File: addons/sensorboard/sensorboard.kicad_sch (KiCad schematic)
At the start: 13 parts, among them J1 Conn_02x06_Odd_Even, J10 Adafruit_I2C_Header, J11 BME680_Header, J12 RGB_Header, J2 SparkFun_I2C_Header, J3 Adafruit_I2C_Header, J4 Pimoroni_I2CGarden_Header, J5 Pimoroni_I2CGarden_Header, J6 Adafruit_I2C_Header, J7 SparkFun_I2C_Header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

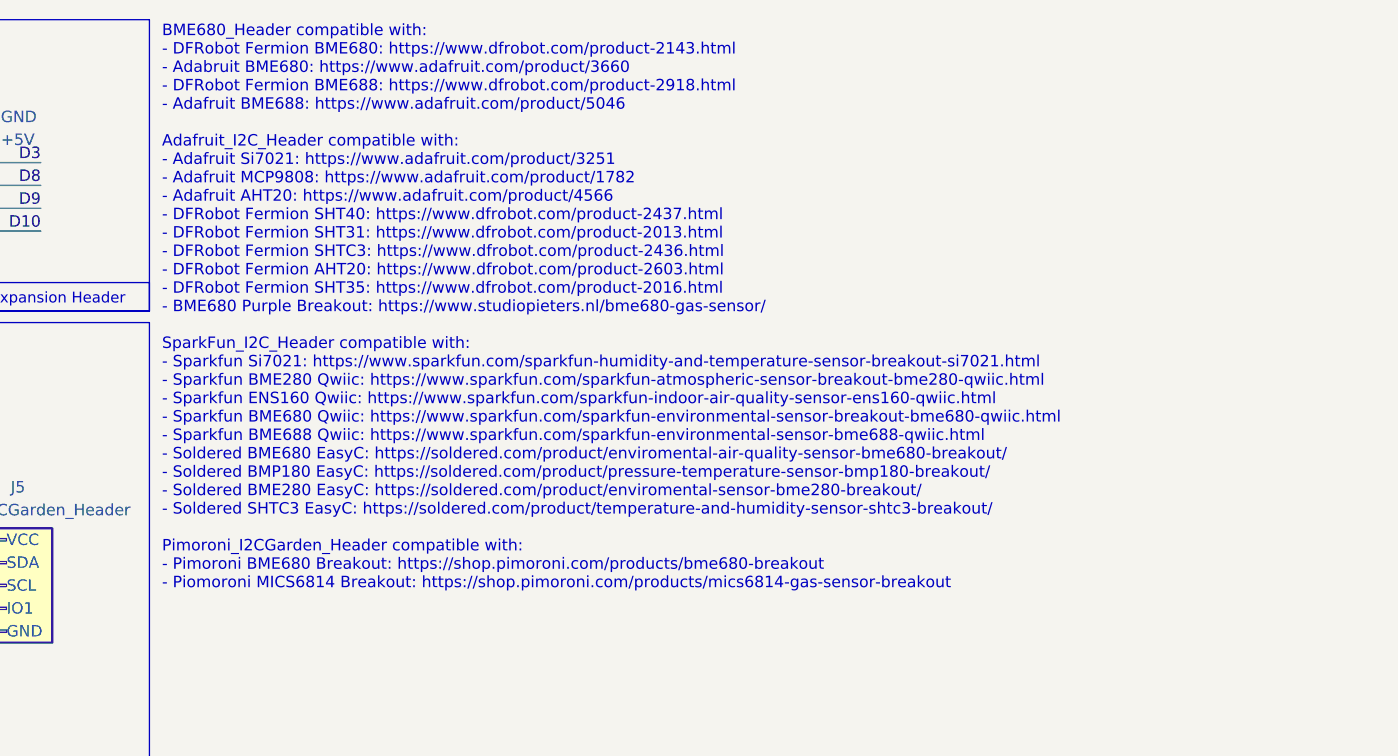
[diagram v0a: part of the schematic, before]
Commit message: More compact version of the AQStation
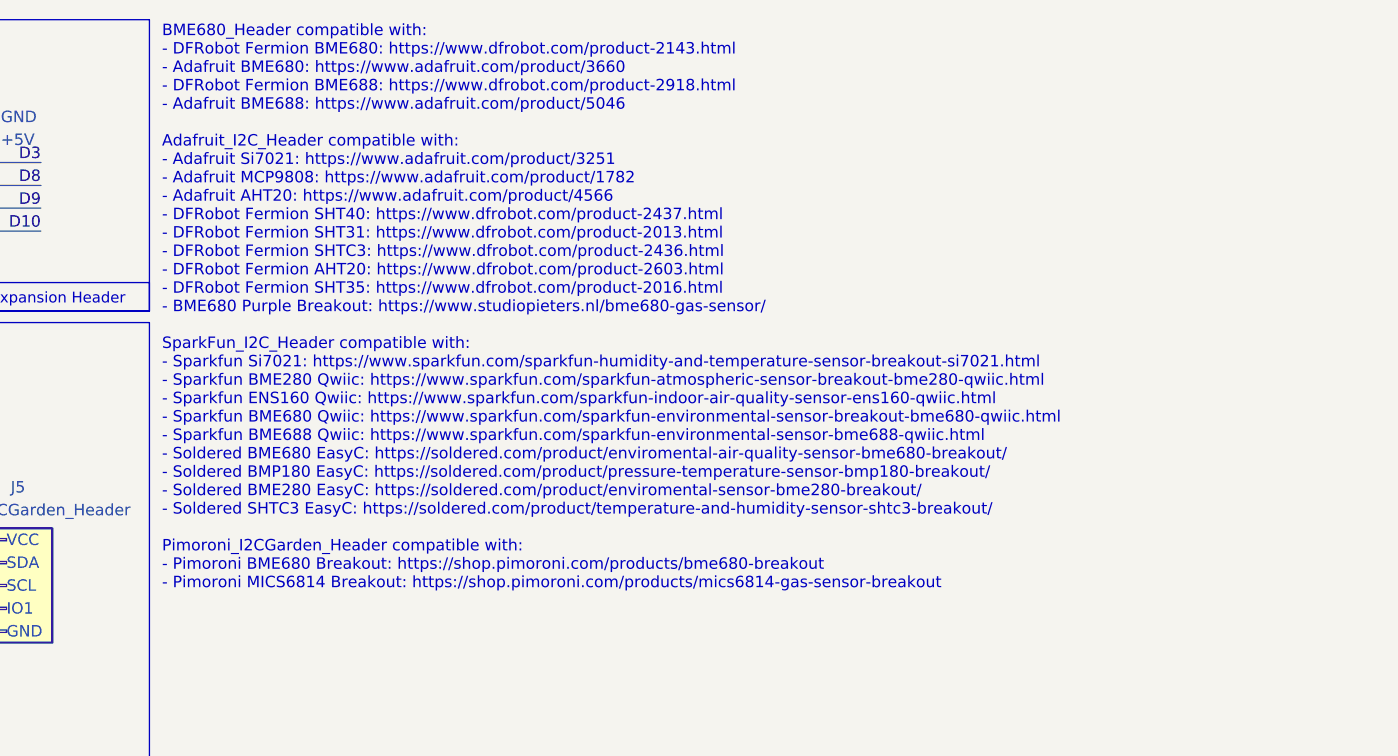
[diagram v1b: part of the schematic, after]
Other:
- note added: "BME680_Header compatible with: - DFRobot Fermion BME680: https://www.dfrobot.com/product-2143.html - Adafruit BME680: https://www.adafruit.com/product/3660 - DFRobot Fermion BME688: https://www.dfrobot.com/product-2918.html - Adafruit BME688: https://www.adafruit.com/product/5046 Adafruit_I2C_Header compatible with: - Adafruit Si7021: https://www.adafruit.com/product/3251 - Adafruit MCP9808: http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"
- note removed: "BME680_Header compatible with: - DFRobot Fermion BME680: https://www.dfrobot.com/product-2143.html - Adabruit BME680: https://www.adafruit.com/product/3660 - DFRobot Fermion BME688: https://www.dfrobot.com/product-2918.html - Adafruit BME688: https://www.adafruit.com/product/5046 Adafruit_I2C_Header compatible with: - Adafruit Si7021: https://www.adafruit.com/product/3251 - Adafruit MCP9808: http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"
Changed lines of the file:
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@@
 		)
 	)
-	(text "BME680_Header compatible with:\n- DFRobot Fermion BME680: https://www.dfrobot.com/product-2143.html\n- Adabruit BME680: https://www.adafruit.com/product/3660\n- DFRobot Fermion BME688: https://www.dfrobot.com/product-2918.html\n- Adafruit BME688: https://www.adafruit.com/product/5046\n\nAdafruit_I2C_Header compatible with:\n- Adafruit Si7021: https://www.adafruit.com/product/3251\n- Adafruit MCP9808: https://www.adafruit.com/product/1782\n- Adafruit AHT20: https://www.adafruit.com/product/4566\n- DFRobot Fermion SHT40: https://www.dfrobot.com/product-2437.html\n- DFRobot Fermion SHT31: https://www.dfrobot.com/product-2013.html\n- DFRobot Fermion SHTC3: https://www.dfrobot.com/product-2436.html\n- DFRobot Fermion AHT20: https://www.dfrobot.com/product-2603.html\n- DFRobot Fermion SHT35: https://www.dfrobot.com/product-2016.html\n- BME680 Purple Breakout: https://www.studiopieters.nl/bme680-gas-sensor/\n\nSparkFun_I2C_Header compatible with:\n- Sparkfun Si7021: https://www.sparkfun.com/sparkfun-humidity-and-temperature-sensor-breakout-si7021.html\n- Sparkfun BME280 Qwiic: https://www.sparkfun.com/sparkfun-atmospheric-sensor-breakout-bme280-qwiic.html\n- Sparkfun ENS160 Qwiic: https://www.sparkfun.com/sparkfun-indoor-air-quality-sensor-ens160-qwiic.html\n- Sparkfun BME680 Qwiic: https://www.sparkfun.com/sparkfun-environmental-sensor-breakout-bme680-qwiic.html\n- Sparkfun BME688 Qwiic: https://www.sparkfun.com/sparkfun-environmental-sensor-bme688-qwiic.html\n- Soldered BME680 EasyC: https://soldered.com/product/enviromental-air-quality-sensor-bme680-breakout/\n- Soldered BMP180 EasyC: https://soldered.com/product/pressure-temperature-sensor-bmp180-breakout/\n- Soldered BME280 EasyC: https://soldered.com/product/enviromental-sensor-bme280-breakout/\n- Soldered SHTC3 EasyC: https://soldered.com/product/temperature-and-humidity-sensor-shtc3-breakout/\n\nPimoroni_I2CGarden_Header compatible with:\n- Pimoroni BME680 Breakout: https://shop.pimoroni.com/products/bme680-breakout\n- Piomoroni MICS6814 Breakout: https://shop.pimoroni.com/products/mics6814-gas-sensor-breakout"
+	(text "BME680_Header compatible with:\n- DFRobot Fermion BME680: https://www.dfrobot.com/product-2143.html\n- Adafruit BME680: https://www.adafruit.com/product/3660\n- DFRobot Fermion BME688: https://www.dfrobot.com/product-2918.html\n- Adafruit BME688: https://www.adafruit.com/product/5046\n\nAdafruit_I2C_Header compatible with:\n- Adafruit Si7021: https://www.adafruit.com/product/3251\n- Adafruit MCP9808: https://www.adafruit.com/product/1782\n- Adafruit AHT20: https://www.adafruit.com/product/4566\n- DFRobot Fermion SHT40: https://www.dfrobot.com/product-2437.html\n- DFRobot Fermion SHT31: https://www.dfrobot.com/product-2013.html\n- DFRobot Fermion SHTC3: https://www.dfrobot.com/product-2436.html\n- DFRobot Fermion AHT20: https://www.dfrobot.com/product-2603.html\n- DFRobot Fermion SHT35: https://www.dfrobot.com/product-2016.html\n- BME680 Purple Breakout: https://www.studiopieters.nl/bme680-gas-sensor/\n\nSparkFun_I2C_Header compatible with:\n- Sparkfun Si7021: https://www.sparkfun.com/sparkfun-humidity-and-temperature-sensor-breakout-si7021.html\n- Sparkfun BME280 Qwiic: https://www.sparkfun.com/sparkfun-atmospheric-sensor-breakout-bme280-qwiic.html\n- Sparkfun ENS160 Qwiic: https://www.sparkfun.com/sparkfun-indoor-air-quality-sensor-ens160-qwiic.html\n- Sparkfun BME680 Qwiic: https://www.sparkfun.com/sparkfun-environmental-sensor-breakout-bme680-qwiic.html\n- Sparkfun BME688 Qwiic: https://www.sparkfun.com/sparkfun-environmental-sensor-bme688-qwiic.html\n- Soldered BME680 EasyC: https://soldered.com/product/enviromental-air-quality-sensor-bme680-breakout/\n- Soldered BMP180 EasyC: https://soldered.com/product/pressure-temperature-sensor-bmp180-breakout/\n- Soldered BME280 EasyC: https://soldered.com/product/enviromental-sensor-bme280-breakout/\n- Soldered SHTC3 EasyC: https://soldered.com/product/temperature-and-humidity-sensor-shtc3-breakout/\n\nPimoroni_I2CGarden_Header compatible with:\n- Pimoroni BME680 Breakout: https://shop.pimoroni.com/products/bme680-breakout\n- Pimoroni MICS6814 Breakout: https://shop.pimoroni.com/products/mics6814-gas-sensor-breakout"
 		(exclude_from_sim no)
 		(at 131.572 13.97 0)

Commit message: Finalize aqstation
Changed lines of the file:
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@@
 		)
 	)
-	(text "BME680_Header compatible with:\n- DFRobot Fermion BME680: https://www.dfrobot.com/product-2143.html\n- Adafruit BME680: https://www.adafruit.com/product/3660\n- DFRobot Fermion BME688: https://www.dfrobot.com/product-2918.html\n- Adafruit BME688: https://www.adafruit.com/product/5046\n\nAdafruit_I2C_Header compatible with:\n- Adafruit Si7021: https://www.adafruit.com/product/3251\n- Adafruit MCP9808: https://www.adafruit.com/product/1782\n- Adafruit AHT20: https://www.adafruit.com/product/4566\n- DFRobot Fermion SHT40: https://www.dfrobot.com/product-2437.html\n- DFRobot Fermion SHT31: https://www.dfrobot.com/product-2013.html\n- DFRobot Fermion SHTC3: https://www.dfrobot.com/product-2436.html\n- DFRobot Fermion AHT20: https://www.dfrobot.com/product-2603.html\n- DFRobot Fermion SHT35: https://www.dfrobot.com/product-2016.html\n- BME680 Purple Breakout: https://www.studiopieters.nl/bme680-gas-sensor/\n\nSparkFun_I2C_Header compatible with:\n- Sparkfun Si7021: https://www.sparkfun.com/sparkfun-humidity-and-temperature-sensor-breakout-si7021.html\n- Sparkfun BME280 Qwiic: https://www.sparkfun.com/sparkfun-atmospheric-sensor-breakout-bme280-qwiic.html\n- Sparkfun ENS160 Qwiic: https://www.sparkfun.com/sparkfun-indoor-air-quality-sensor-ens160-qwiic.html\n- Sparkfun BME680 Qwiic: https://www.sparkfun.com/sparkfun-environmental-sensor-breakout-bme680-qwiic.html\n- Sparkfun BME688 Qwiic: https://www.sparkfun.com/sparkfun-environmental-sensor-bme688-qwiic.html\n- Soldered BME680 EasyC: https://soldered.com/product/enviromental-air-quality-sensor-bme680-breakout/\n- Soldered BMP180 EasyC: https://soldered.com/product/pressure-temperature-sensor-bmp180-breakout/\n- Soldered BME280 EasyC: https://soldered.com/product/enviromental-sensor-bme280-breakout/\n- Soldered SHTC3 EasyC: https://soldered.com/product/temperature-and-humidity-sensor-shtc3-breakout/\n\nPimoroni_I2CGarden_Header compatible with:\n- Pimoroni BME680 Breakout: https://shop.pimoroni.com/products/bme680-breakout\n- Pimoroni MICS6814 Breakout: https://shop.pimoroni.com/products/mics6814-gas-sensor-breakout"
+	(text "BME680_Header compatible with:\n- DFRobot Fermion BME680: https://www.dfrobot.com/product-2143.html\n- Adafruit BME680: https://www.adafruit.com/product/3660\n- DFRobot Fermion BME688: https://www.dfrobot.com/product-2918.html\n- Adafruit BME688: https://www.adafruit.com/product/5046\n\nAdafruit_I2C_Header compatible with:\n- Adafruit Si7021: https://www.adafruit.com/product/3251\n- Adafruit MCP9808: https://www.adafruit.com/product/1782\n- Adafruit AHT20: https://www.adafruit.com/product/4566\n- DFRobot Fermion SHT40: https://www.dfrobot.com/product-2437.html\n- DFRobot Fermion SHT31: https://www.dfrobot.com/product-2013.html\n- DFRobot Fermion SHTC3: https://www.dfrobot.com/product-2436.html\n- DFRobot Fermion AHT20: https://www.dfrobot.com/product-2603.html\n- DFRobot Fermion SHT35: https://www.dfrobot.com/product-2016.html\n- BME680 Purple Breakout: https://www.studiopieters.nl/bme680-gas-sensor/\n\nSparkFun_I2C_Header compatible with:\n- Sparkfun Si7021: https://www.sparkfun.com/sparkfun-humidity-and-temperature-sensor-breakout-si7021.html\n- Sparkfun BME280 Qwiic: https://www.sparkfun.com/sparkfun-atmospheric-sensor-breakout-bme280-qwiic.html\n- Sparkfun ENS160 Qwiic: https://www.sparkfun.com/sparkfun-indoor-air-quality-sensor-ens160-qwiic.html\n- Sparkfun BME680 Qwiic: https://www.sparkfun.com/sparkfun-environmental-sensor-breakout-bme680-qwiic.html\n- Sparkfun BME688 Qwiic: https://www.sparkfun.com/sparkfun-environmental-sensor-bme688-qwiic.html\n- Soldered BME680 EasyC: https://soldered.com/product/enviromental-air-quality-sensor-bme680-breakout/\n- Soldered BMP180 EasyC: https://soldered.com/product/pressure-temperature-sensor-bmp180-breakout/\n- Soldered BME280 EasyC: https://soldered.com/product/enviromental-sensor-bme280-breakout/\n- Soldered SHTC3 EasyC: https://soldered.com/product/temperature-and-humidity-sensor-shtc3-breakout/\n\nPimoroni_I2CGarden_Header compatible with:\n- Pimoroni BME680 Breakout: https://shop.pimoroni.com/products/bme680-breakout\n- Pimoroni MICS6814 Breakout: https://shop.pimoroni.com/products/mics6814-gas-sensor-breakout\n\nST/Qwiic Connector compatible with\n- Qwiic sensors: https://www.sparkfun.com/qwiic\n- STEMMA QT sensors: https://learn.adafruit.com/introducing-adafruit-stemma-qt/what-is-stemma-qt\n- easyC sensors: https://soldered.com/easyC/"
 		(exclude_from_sim no)
-		(at 131.572 13.97 0)
+		(at 131.572 14.732 0)
 		(effects
 			(font

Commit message: Fix issues with the initial version and add support for DFRobot BME breakouts
Update documentation
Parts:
- J11: value BME680_Header -> Adafruit_BME680_Header; footprint Header:BME680_Header -> Header:Adafruit_BME680_Header; symbol Header:BME680_Header -> Header:Adafruit_BME680_Header
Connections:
- net D6: now also J11.5 (SDO)
- net D7: now also J11.7 (CS)
- no-connect marks 9 -> 7
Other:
- note added: "Adafruit_BME680_Header compatible with: - Adafruit BME280: https://www.adafruit.com/product/2652 - Adafruit BME680: https://www.adafruit.com/product/3660 - Adafruit BME688: https://www.adafruit.com/product/5046 Adafruit_I2C_Header compatible with: - Adafruit Si7021: https://www.adafruit.com/product/3251 - Adafruit MCP9808: https://www.adafruit.com/product/1782 - Adafruit AHT20: https://www.adafru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"
- note removed: "BME680_Header compatible with: - DFRobot Fermion BME680: https://www.dfrobot.com/product-2143.html - Adafruit BME680: https://www.adafruit.com/product/3660 - DFRobot Fermion BME688: https://www.dfrobot.com/product-2918.html - Adafruit BME688: https://www.adafruit.com/product/5046 Adafruit_I2C_Header compatible with: - Adafruit Si7021: https://www.adafruit.com/product/3251 - Adafruit MCP9808: http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"
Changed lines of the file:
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@@
 		)
 	)
-	(text "BME680_Header compatible with:\n- DFRobot Fermion BME680: https://www.dfrobot.com/product-2143.html\n- Adafruit BME680: https://www.adafruit.com/product/3660\n- DFRobot Fermion BME688: https://www.dfrobot.com/product-2918.html\n- Adafruit BME688: https://www.adafruit.com/product/5046\n\nAdafruit_I2C_Header compatible with:\n- Adafruit Si7021: https://www.adafruit.com/product/3251\n- Adafruit MCP9808: https://www.adafruit.com/product/1782\n- Adafruit AHT20: https://www.adafruit.com/product/4566\n- DFRobot Fermion SHT40: https://www.dfrobot.com/product-2437.html\n- DFRobot Fermion SHT31: https://www.dfrobot.com/product-2013.html\n- DFRobot Fermion SHTC3: https://www.dfrobot.com/product-2436.html\n- DFRobot Fermion AHT20: https://www.dfrobot.com/product-2603.html\n- DFRobot Fermion SHT35: https://www.dfrobot.com/product-2016.html\n- BME680 Purple Breakout: https://www.studiopieters.nl/bme680-gas-sensor/\n\nSparkFun_I2C_Header compatible with:\n- Sparkfun Si7021: https://www.sparkfun.com/sparkfun-humidity-and-temperature-sensor-breakout-si7021.html\n- Sparkfun BME280 Qwiic: https://www.sparkfun.com/sparkfun-atmospheric-sensor-breakout-bme280-qwiic.html\n- Sparkfun ENS160 Qwiic: https://www.sparkfun.com/sparkfun-indoor-air-quality-sensor-ens160-qwiic.html\n- Sparkfun BME680 Qwiic: https://www.sparkfun.com/sparkfun-environmental-sensor-breakout-bme680-qwiic.html\n- Sparkfun BME688 Qwiic: https://www.sparkfun.com/sparkfun-environmental-sensor-bme688-qwiic.html\n- Soldered BME680 EasyC: https://soldered.com/product/enviromental-air-quality-sensor-bme680-breakout/\n- Soldered BMP180 EasyC: https://soldered.com/product/pressure-temperature-sensor-bmp180-breakout/\n- Soldered BME280 EasyC: https://soldered.com/product/enviromental-sensor-bme280-breakout/\n- Soldered SHTC3 EasyC: https://soldered.com/product/temperature-and-humidity-sensor-shtc3-breakout/\n\nPimoroni_I2CGarden_Header compatible with:\n- Pimoroni BME680 Breakout: https://shop.pimoroni.com/products/bme680-breakout\n- Pimoroni MICS6814 Breakout: https://shop.pimoroni.com/products/mics6814-gas-sensor-breakout\n\nST/Qwiic Connector compatible with\n- Qwiic sensors: https://www.sparkfun.com/qwiic\n- STEMMA QT sensors: https://learn.adafruit.com/introducing-adafruit-stemma-qt/what-is-stemma-qt\n- easyC sensors: https://soldered.com/easyC/"
+	(text "Adafruit_BME680_Header compatible with:\n- Adafruit BME280: https://www.adafruit.com/product/2652\n- Adafruit BME680: https://www.adafruit.com/product/3660\n- Adafruit BME688: https://www.adafruit.com/product/5046\n\nAdafruit_I2C_Header compatible with:\n- Adafruit Si7021: https://www.adafruit.com/product/3251\n- Adafruit MCP9808: https://www.adafruit.com/product/1782\n- Adafruit AHT20: https://www.adafruit.com/product/4566\n- DFRobot Fermion SHT40: https://www.dfrobot.com/product-2437.html\n- DFRobot Fermion SHT31: https://www.dfrobot.com/product-2013.html\n- DFRobot Fermion SHTC3: https://www.dfrobot.com/product-2436.html\n- DFRobot Fermion AHT20: https://www.dfrobot.com/product-2603.html\n- DFRobot Fermion SHT35: https://www.dfrobot.com/product-2016.html\n- BME680 Purple Breakout: https://www.studiopieters.nl/bme680-gas-sensor/\n\nSparkFun_I2C_Header compatible with:\n- Sparkfun Si7021: https://www.sparkfun.com/sparkfun-humidity-and-temperature-sensor-breakout-si7021.html\n- Sparkfun BME280 Qwiic: https://www.sparkfun.com/sparkfun-atmospheric-sensor-breakout-bme280-qwiic.html\n- Sparkfun ENS160 Qwiic: https://www.sparkfun.com/sparkfun-indoor-air-quality-sensor-ens160-qwiic.html\n- Sparkfun BME680 Qwiic: https://www.sparkfun.com/sparkfun-environmental-sensor-breakout-bme680-qwiic.html\n- Sparkfun BME688 Qwiic: https://www.sparkfun.com/sparkfun-environmental-sensor-bme688-qwiic.html\n- Soldered BME680 EasyC: https://soldered.com/product/enviromental-air-quality-sensor-bme680-breakout/\n- Soldered BMP180 EasyC: https://soldered.com/product/pressure-temperature-sensor-bmp180-breakout/\n- Soldered BME280 EasyC: https://soldered.com/product/enviromental-sensor-bme280-breakout/\n- Soldered SHTC3 EasyC: https://soldered.com/product/temperature-and-humidity-sensor-shtc3-breakout/\n\nPimoroni_I2CGarden_Header compatible with:\n- Pimoroni BME680 Breakout: https://shop.pimoroni.com/products/bme680-breakout\n- Pimoroni MICS6814 Breakout: https://shop.pimoroni.com/products/mics6814-gas-sensor-breakout\n\nST/Qwiic Connector compatible with\n- Qwiic sensors: https://www.sparkfun.com/qwiic\n- STEMMA QT sensors: https://learn.adafruit.com/introducing-adafruit-stemma-qt/what-is-stemma-qt\n- easyC sensors: https://soldered.com/easyC/"
 		(exclude_from_sim no)
 		(at 131.572 14.732 0)
@@
 	)
 	(no_connect
-		(at 63.5 123.19)
-	)
-	(no_connect
-		(at 63.5 118.11)
-	)
-	(no_connect
 		(at 80.01 63.5)
 	)
@@
 	(wire
 		(pts
+			(xy 63.5 123.19) (xy 71.12 123.19)
+		)
+		(stroke
+			(width 0)
+			(type default)
+		)
+	)
+	(wire
+		(pts
 			(xy 58.42 63.5) (xy 58.42 71.12)
 		)
@@
 		(pts
 			(xy 55.88 33.02) (xy 63.5 33.02)
+		)
+		(stroke
+			(width 0)
+			(type default)
+		)
+	)
+	(wire
+		(pts
+			(xy 63.5 118.11) (xy 71.12 118.11)
 		)
 		(stroke
@@
 		)
 	)
+	(label "D6"
+		(at 71.12 123.19 180)
+		(effects
+			(font
+				(size 1.27 1.27)
+			)
+			(justify right bottom)
+		)
+	)
 	(label "SDA"
 		(at 90.17 71.12 90)
@@
 	(label "D8"
 		(at 85.09 80.01 270)
+		(effects
+			(font
+				(size 1.27 1.27)
+			)
+			(justify right bottom)
+		)
+	)
+	(label "D7"
+		(at 71.12 118.11 180)
 		(effects
 			(font
@@
 	)
 	(symbol
-		(lib_id "Header:BME680_Header")
+		(lib_id "Header:Adafruit_BME680_Header")
 		(at 57.15 125.73 180)
 		(unit 1)
@@
 		(dnp no)
 		(property "Reference" "J11"
-			(at 53.594 113.284 0)
+			(at 53.34 113.284 0)
 			(effects
 				(font
@@
 			)
 		)
-		(property "Value" "BME680_Header"
+		(property "Value" "Adafruit_BME680_Header"
 			(at 53.34 115.316 0)
 			(effects
@@
 			)
 		)
-		(property "Footprint" "Header:BME680_Header"
+		(property "Footprint" "Header:Adafruit_BME680_Header"
 			(at 57.15 125.73 0)
 			(effects
